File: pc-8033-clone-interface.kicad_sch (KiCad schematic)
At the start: 5 parts, among them U2 74LS32, U3 74LS04, U4 82C55A, U5 74LS30

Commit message: Now we're getting into the troubles
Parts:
- added J1: PC-80S31, symbol Connector_Generic:Conn_02x17_Odd_Even
- added TP1: +5V, symbol Connector:TestPoint
- added TP2: GND, symbol Connector:TestPoint
- added unit 2 of U3
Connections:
- net +5V: now also TP1.1
- net GND: now also J1.17 (Pin_17), J1.19 (Pin_19), J1.21 (Pin_21), J1.23 (Pin_23), J1.25 (Pin_25), J1.27 (Pin_27), J1.29 (Pin_29), J1.31 (Pin_31), J1.33 (Pin_33), TP2.1
- net RESET: now also U3.3
- net pa3: now reaches U4.1 (PA3)
- net pa3: now also J1.8 (Pin_8)
- net pc7: now reaches U4.10 (PC7)
- net pc7: now also J1.24 (Pin_24)
- net pc6: now reaches U4.11 (PC6)
- net pc6: now also J1.22 (Pin_22)
- net pc5: now reaches U4.12 (PC5)
- net pc5: now also J1.20 (Pin_20)
- net pc4: now reaches U4.13 (PC4)
- net pc4: now also J1.18 (Pin_18)
- net pc0: now reaches U4.14 (PC0)
- net pc0: now also J1.26 (Pin_26)
- net pc1: now reaches U4.15 (PC1)
- net pc1: now also J1.28 (Pin_28)
- net pc2: now reaches U4.16 (PC2)
- net pc2: now also J1.30 (Pin_30)
- net pc3: now reaches U4.17 (PC3)
- net pc3: now also J1.32 (Pin_32)
- net at U4.18 (PB0): now also J1.1 (Pin_1)
- net at U4.19 (PB1): now also J1.3 (Pin_3)
- net pa2: now reaches U4.2 (PA2)
- net pa2: now also J1.6 (Pin_6)
- net at U4.20 (PB2): now also J1.5 (Pin_5)
- net at U4.21 (PB3): now also J1.7 (Pin_7)
- net at U4.22 (PB4): now also J1.9 (Pin_9)
- net at U4.23 (PB5): now also J1.11 (Pin_11)
- net at U4.24 (PB6): now also J1.13 (Pin_13)
- net at U4.25 (PB7): now also J1.15 (Pin_15)
- net pa1: now reaches U4.3 (PA1)
- net pa1: now also J1.4 (Pin_4)
- net pa7: now reaches U4.37 (PA7)
- net pa7: now also J1.16 (Pin_16)
- net pa6: now reaches U4.38 (PA6)
- net pa6: now also J1.14 (Pin_14)
- net pa5: now reaches U4.39 (PA5)
- net pa5: now also J1.12 (Pin_12)
- net pa0: now reaches U4.4 (PA0)
- net pa0: now also J1.2 (Pin_2)
- net pa4: now reaches U4.40 (PA4)
- net pa4: now also J1.10 (Pin_10)
- new net: J1.34 (Pin_34), U3.4
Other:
- note added: "TODO: Pull-up? down? resistors? 4.7k? Which lines?"
- note added: "TODO: there is something special to do about exton"
- note added: "This second inversion of reset appears to be important for timing purposes, as per https://blog.goo.ne.jp/tk-80/e/6ac4226f93ae2f80224ee7fcf31cb796"
- note added: "https://electrelic.com/electrelic/node/330"

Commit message: Reset faffing
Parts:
- added R1: 4.7kΩ, Resistor_THT:R_Axial_DIN0309_L9.0mm_D3.2mm_P12.70mm_Horizontal, symbol Device:R_Small_US
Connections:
- net +5V: now also R1.1
- net at J1.34 (Pin_34), U3.4: now also R1.2
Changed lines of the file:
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@@
   (junction (at 173.99 121.92) (diameter 0) (color 0 0 0 0)
+  )
+  (junction (at 206.375 139.065) (diameter 0) (color 0 0 0 0)
   )
   (junction (at 173.99 114.3) (diameter 0) (color 0 0 0 0)
@@
     (stroke (width 0) (type default))
   )
+  (wire (pts (xy 219.71 133.985) (xy 219.71 124.46))
+    (stroke (width 0) (type default))
+  )
   (wire (pts (xy 44.45 86.36) (xy 44.45 103.505))
     (stroke (width 0) (type default))
@@
     (stroke (width 0) (type default))
   )
-  (wire (pts (xy 206.375 148.59) (xy 206.375 129.54))
+  (wire (pts (xy 206.375 148.59) (xy 206.375 139.065))
     (stroke (width 0) (type default))
   )
@@
     (stroke (width 0) (type default))
   )
+  (wire (pts (xy 206.375 139.065) (xy 206.375 129.54))
+    (stroke (width 0) (type default))
+  )
   (wire (pts (xy 156.845 78.74) (xy 160.02 78.74))
     (stroke (width 0) (type default))
@@
   )
   (wire (pts (xy 196.85 129.54) (xy 206.375 129.54))
+    (stroke (width 0) (type default))
+  )
+  (wire (pts (xy 206.375 139.065) (xy 219.71 139.065))
     (stroke (width 0) (type default))
   )
@@
         )
       )
+    )
+  )
+  (symbol (lib_id "Device:R_Small_US") (at 219.71 136.525 0) (unit 1)
+    (in_bom yes) (on_board yes) (dnp no) (fields_autoplaced)
+    (property "Reference" "R1" (at 222.25 135.255 0)
+      (effects (font (size 1.27 1.27)) (justify left))
+    )
+    (property "Value" "4.7kΩ" (at 222.25 137.795 0)
+      (effects (font (size 1.27 1.27)) (justify left))
+    )
+    (property "Footprint" "Resistor_THT:R_Axial_DIN0309_L9.0mm_D3.2mm_P12.70mm_Horizontal" (at 219.71 136.525 0)
+      (effects (font (size 1.27 1.27)) hide)
+    )
+    (property "Datasheet" "~" (at 219.71 136.525 0)
+      (effects (font (size 1.27 1.27)) hide)
+    )
+    (pin "1")
+    (pin "2")
+    (instances
+      (project "pc-8033-clone-interface"
+        (path "/9d504855-0dbe-4626-9ba5-7c5a4a75c091"
+          (reference "R1") (unit 1)
+        )
+      )
+    )
+  )
+  (symbol (lib_id "power:+5V") (at 219.71 124.46 0) (unit 1)
+    (in_bom yes) (on_board yes) (dnp no) (fields_autoplaced)
+    (property "Reference" "#PWR015" (at 219.71 128.27 0)
+      (effects (font (size 1.27 1.27)) hide)
+    )
+    (property "Value" "+5V" (at 219.71 119.38 0)
+      (effects (font (size 1.27 1.27)))
+    )
+    (property "Footprint" "" (at 219.71 124.46 0)
+      (effects (font (size 1.27 1.27)) hide)
+    )
+    (property "Datasheet" "" (at 219.71 124.46 0)
+      (effects (font (size 1.27 1.27)) hide)
+    )
+    (pin "1")
+    (instances
+      (project "pc-8033-clone-interface"
+        (path "/9d504855-0dbe-4626-9ba5-7c5a4a75c091"
+          (reference "#PWR015") (unit 1)
+        )
+      )

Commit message: EXTON strapped low
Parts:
- added R2: 4.7kΩ, Resistor_THT:R_Axial_DIN0309_L9.0mm_D3.2mm_P12.70mm_Horizontal, symbol Device:R_Small_US
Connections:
- net GND: now also R2.2
- net at U1.18 (~{EXTON}): now also R2.1
- no-connect marks 27 -> 26
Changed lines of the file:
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@@
   (no_connect (at 46.355 99.06))
   (no_connect (at 46.355 68.58))
-  (no_connect (at 46.355 81.28))
   (no_connect (at 46.355 78.74))
   (no_connect (at 46.355 116.84))
@@
     (stroke (width 0) (type default))
   )
+  (wire (pts (xy 46.355 81.28) (xy 38.1 81.28))
+    (stroke (width 0) (type default))
+  )
   (wire (pts (xy 196.85 104.14) (xy 206.375 104.14))
     (stroke (width 0) (type default))
@@
     (stroke (width 0) (type default))
   )
+  (wire (pts (xy 27.94 58.42) (xy 27.94 62.23))
+    (stroke (width 0) (type default))
+  )
   (wire (pts (xy 173.99 127) (xy 173.99 124.46))
     (stroke (width 0) (type default))
@@
     (stroke (width 0) (type default))
   )
+  (wire (pts (xy 38.1 58.42) (xy 38.1 81.28))
+    (stroke (width 0) (type default))
+  )
   (wire (pts (xy 173.99 124.46) (xy 173.99 121.92))
     (stroke (width 0) (type default))
@@
   )
   (wire (pts (xy 156.845 91.44) (xy 184.15 91.44))
+    (stroke (width 0) (type default))
+  )
+  (wire (pts (xy 38.1 58.42) (xy 27.94 58.42))
     (stroke (width 0) (type default))
   )
@@
         (path "/9d504855-0dbe-4626-9ba5-7c5a4a75c091"
           (reference "#FLG02") (unit 1)
+        )
+      )
+    )
+  )
+  (symbol (lib_id "Device:R_Small_US") (at 27.94 64.77 0) (unit 1)
+    (in_bom yes) (on_board yes) (dnp no) (fields_autoplaced)
+    (property "Reference" "R2" (at 30.48 63.5 0)
+      (effects (font (size 1.27 1.27)) (justify left))
+    )
+    (property "Value" "4.7kΩ" (at 30.48 66.04 0)
+      (effects (font (size 1.27 1.27)) (justify left))
+    )
+    (property "Footprint" "Resistor_THT:R_Axial_DIN0309_L9.0mm_D3.2mm_P12.70mm_Horizontal" (at 27.94 64.77 0)
+      (effects (font (size 1.27 1.27)) hide)
+    )
+    (property "Datasheet" "~" (at 27.94 64.77 0)
+      (effects (font (size 1.27 1.27)) hide)
+    )
+    (pin "1")
+    (pin "2")
+    (instances
+      (project "pc-8033-clone-interface"
+        (path "/9d504855-0dbe-4626-9ba5-7c5a4a75c091"
+          (reference "R2") (unit 1)
         )
       )
@@
         )
       )
+    )
+  )
+  (symbol (lib_id "power:GND") (at 27.94 67.31 0) (unit 1)
+    (in_bom yes) (on_board yes) (dnp no) (fields_autoplaced)
+    (property "Reference" "#PWR016" (at 27.94 73.66 0)
+      (effects (font (size 1.27 1.27)) hide)
+    )
+    (property "Value" "GND" (at 27.94 72.39 0)
+      (effects (font (size 1.27 1.27)))
+    )
+    (property "Footprint" "" (at 27.94 67.31 0)
+      (effects (font (size 1.27 1.27)) hide)
+    )
+    (property "Datasheet" "" (at 27.94 67.31 0)
+      (effects (font (size 1.27 1.27)) hide)
+    )
+    (pin "1")
+    (instances
+      (project "pc-8033-clone-interface"
+        (path "/9d504855-0dbe-4626-9ba5-7c5a4a75c091"
+          (reference "#PWR016") (unit 1)
+        )
+      )

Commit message: Pull-downs
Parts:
- added C1: 220µF, Capacitor_THT:CP_Radial_D6.3mm_P2.50mm, symbol Device:C_Polarized_Small_US
- added JP1: Jumper_2_Bridged, Jumper:SolderJumper-2_P1.3mm_Bridged2Bar_Pad1.0x1.5mm, symbol Jumper:Jumper_2_Bridged
- added RN1, RN2, RN3: R_Network08_US, Resistor_THT:R_Array_SIP9, symbol Device:R_Network08_US
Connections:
- net +5V: now also C1.1
- net GND: now also C1.2, JP1.1 (A)
- net pa0: now also RN1.2 (R1)
- net pa1: now also RN1.3 (R2)
- net pa2: now also RN1.4 (R3)
- net pa3: now also RN1.5 (R4)
- net pa4: now also RN1.6 (R5)
- net pa5: now also RN1.7 (R6)
- net pa6: now also RN1.8 (R7)
- net pa7: now also RN1.9 (R8)
- net pc0: now also RN3.2 (R1)
- net pc1: now also RN3.3 (R2)
- net pc2: now also RN3.4 (R3)
- net pc3: now also RN3.5 (R4)
- net pc4: now also RN3.6 (R5)
- net pc5: now also RN3.7 (R6)
- net pc6: now also RN3.8 (R7)
- net pc7: now also RN3.9 (R8)
- net pb0: now reaches J1.1 (Pin_1), U4.18 (PB0)
- net pb0: now also RN2.2 (R1)
- net pb1: now reaches J1.3 (Pin_3), U4.19 (PB1)
- net pb1: now also RN2.3 (R2)
- net pb2: now reaches J1.5 (Pin_5), U4.20 (PB2)
- net pb2: now also RN2.4 (R3)
- net pb3: now reaches J1.7 (Pin_7), U4.21 (PB3)
- net pb3: now also RN2.5 (R4)
- net pb4: now reaches J1.9 (Pin_9), U4.22 (PB4)
- net pb4: now also RN2.6 (R5)
- net pb5: now reaches J1.11 (Pin_11), U4.23 (PB5)
- net pb5: now also RN2.7 (R6)
- net pb6: now reaches J1.13 (Pin_13), U4.24 (PB6)
- net pb6: now also RN2.8 (R7)
- net pb7: now reaches J1.15 (Pin_15), U4.25 (PB7)
- net pb7: now also RN2.9 (R8)
- new net: JP1.2 (B), RN1.1 (common), RN2.1 (common), RN3.1 (common)
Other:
- note added: "TODO: why is the other blog entry 36 pin when the real 8033 is 34"
- note removed: "TODO: Pull-up? down? resistors? 4.7k? Which lines?"
- note removed: "TODO: there is something special to do about exton"

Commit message: Capture dual footprint IDC header
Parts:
- removed J1: PC-80S31, symbol Connector_Generic:Conn_02x17_Odd_Even
- added J2: 80s31, symbol Connector_Generic:Conn_02x18_Odd_Even
- RN1, RN2, RN3: value R_Network08_US -> 4.7kΩ
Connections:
- net GND: now also J2.17 (Pin_17), J2.19 (Pin_19), J2.21 (Pin_21), J2.23 (Pin_23), J2.25 (Pin_25), J2.27 (Pin_27), J2.29 (Pin_29), J2.31 (Pin_31), J2.33 (Pin_33), J2.35 (Pin_35), J2.36 (Pin_36)
- net pa0: now also J2.2 (Pin_2)
- net pa1: now also J2.4 (Pin_4)
- net pa2: now also J2.6 (Pin_6)
- net pa3: now also J2.8 (Pin_8)
- net pa4: now also J2.10 (Pin_10)
- net pa5: now also J2.12 (Pin_12)
- net pa6: now also J2.14 (Pin_14)
- net pa7: now also J2.16 (Pin_16)
- net pb0: now also J2.1 (Pin_1)
- net pb1: now also J2.3 (Pin_3)
- net pb2: now also J2.5 (Pin_5)
- net pb3: now also J2.7 (Pin_7)
- net pb4: now also J2.9 (Pin_9)
- net pb5: now also J2.11 (Pin_11)
- net pb6: now also J2.13 (Pin_13)
- net pb7: now also J2.15 (Pin_15)
- net pc0: now also J2.26 (Pin_26)
- net pc1: now also J2.28 (Pin_28)
- net pc2: now also J2.30 (Pin_30)
- net pc3: now also J2.32 (Pin_32)
- net pc4: now also J2.18 (Pin_18)
- net pc5: now also J2.20 (Pin_20)
- net pc6: now also J2.22 (Pin_22)
- net pc7: now also J2.24 (Pin_24)
- net at R1.2, U3.4: now also J2.34 (Pin_34)
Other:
- note added: "34 pin (8031): https://electrelic.com/electrelic/node/330 36 pin (80S31): https://electrelic.com/electrelic/node/268"
- note added: "TODO: Maybe add a disable switch?"
- note added: "TODO: Redo for 80S31 seems like we can do a dual footprint https://electrelic.com/electrelic/node/268"
- note removed: "TODO: why is the other blog entry 36 pin when the real 8033 is 34"
- note removed: "https://electrelic.com/electrelic/node/330"

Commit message: Clean up stale TODO
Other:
- note removed: "TODO: Redo for 80S31 seems like we can do a dual footprint https://electrelic.com/electrelic/node/268"
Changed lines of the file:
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@@
-    (effects (font (size 1.27 1.27)) (justify left bottom))
-  )
-  (text "TODO: Redo for 80S31\n\nseems like we can do a dual footprint\n\nhttps://electrelic.com/electrelic/node/268"
-    (at 229.87 110.49 0)
     (effects (font (size 1.27 1.27)) (justify left bottom))
   )

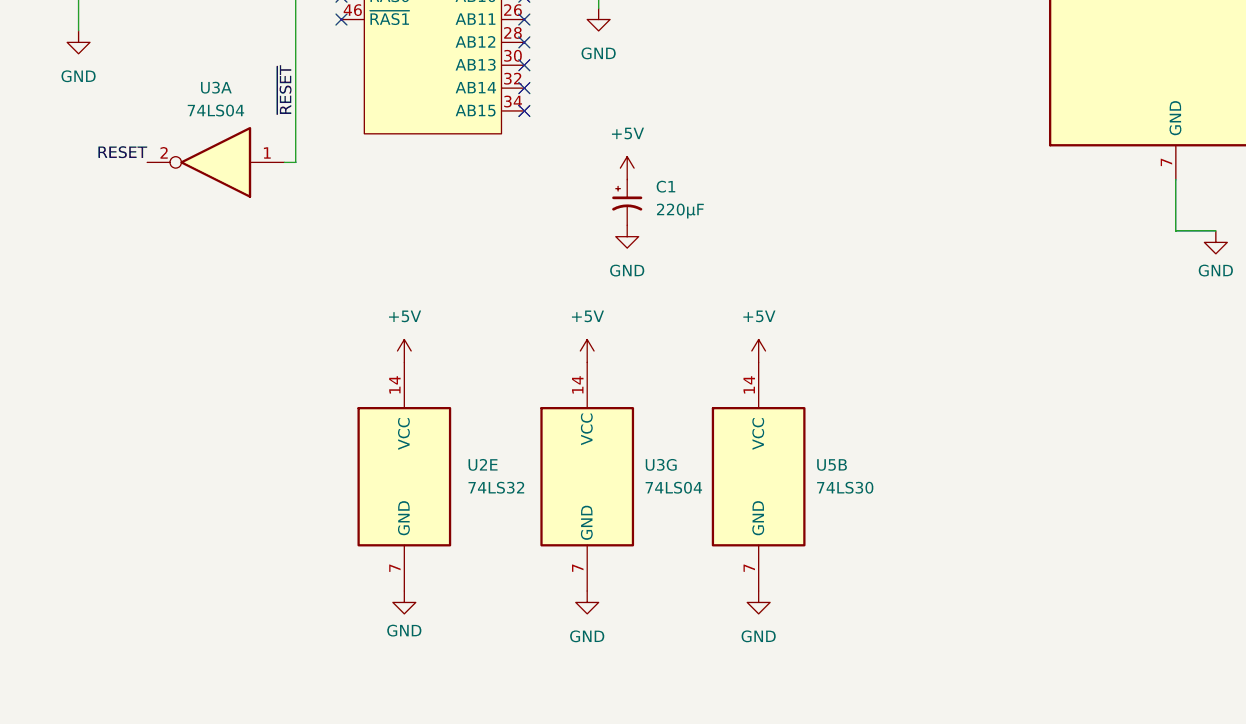
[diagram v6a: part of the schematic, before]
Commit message: Clean up schem warnings
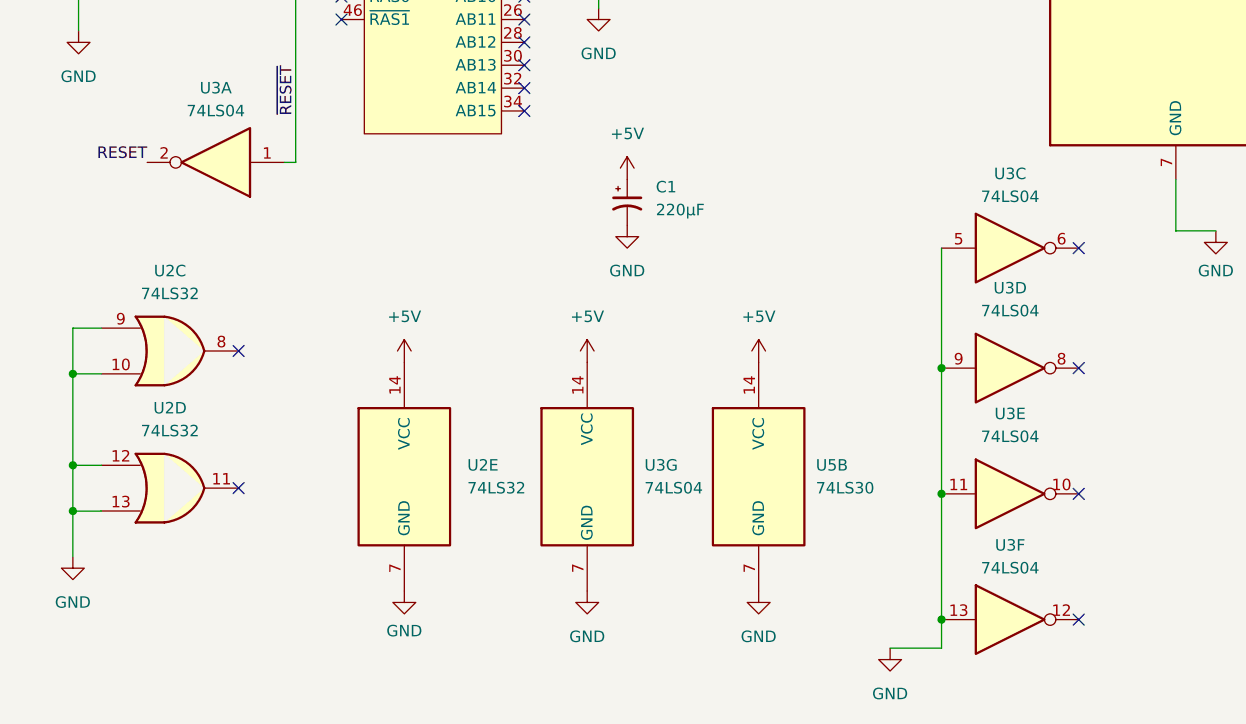
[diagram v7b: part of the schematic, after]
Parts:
- added unit 4 of U2
- added unit 3 of U2
- added unit 6 of U3
- added unit 3 of U3
- added unit 5 of U3
- added unit 4 of U3
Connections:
- net GND: now also U2.10, U2.12, U2.13, U2.9, U3.11, U3.13, U3.5, U3.9
- no-connect marks 26 -> 32

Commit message: Lots of clearance issues...
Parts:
- J2: footprint (none) -> Connector_PinHeader_2.54mm:PinHeader_2x18_P2.54mm_Vertical
- TP1, TP2: footprint (none) -> TestPoint:TestPoint_Loop_D1.80mm_Drill1.0mm_Beaded
- U1: footprint (none) -> Connector_PinHeader_2.54mm:PinHeader_2x25_P2.54mm_Vertical
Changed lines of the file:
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@@
       (effects (font (size 1.27 1.27)) (justify left))
     )
-    (property "Footprint" "" (at 177.165 31.115 0)
+    (property "Footprint" "TestPoint:TestPoint_Loop_D1.80mm_Drill1.0mm_Beaded" (at 177.165 31.115 0)
       (effects (font (size 1.27 1.27)) hide)
     )
@@
       (effects (font (size 1.27 1.27)))
     )
-    (property "Footprint" "" (at 64.135 63.5 0)
+    (property "Footprint" "Connector_PinHeader_2.54mm:PinHeader_2x25_P2.54mm_Vertical" (at 64.135 63.5 0)
       (effects (font (size 1.27 1.27)) hide)
     )
@@
       (effects (font (size 1.27 1.27)) (justify left))
     )
-    (property "Footprint" "" (at 177.165 43.815 0)
+    (property "Footprint" "TestPoint:TestPoint_Loop_D1.80mm_Drill1.0mm_Beaded" (at 177.165 43.815 0)
       (effects (font (size 1.27 1.27)) hide)
     )
@@
       (effects (font (size 1.27 1.27)))
     )
-    (property "Footprint" "" (at 189.23 109.22 0)
-      (effects (font (size 1.27 1.27)) hide)
-    )
+    (property "Footprint" "Connector_PinHeader_2.54mm:PinHeader_2x18_P2.54mm_Vertical" (at 189.23 109.22 0)
+      (effects (font (size 1.27 1.27)) hide)
+    )
